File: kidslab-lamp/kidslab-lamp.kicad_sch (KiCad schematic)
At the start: 1 part

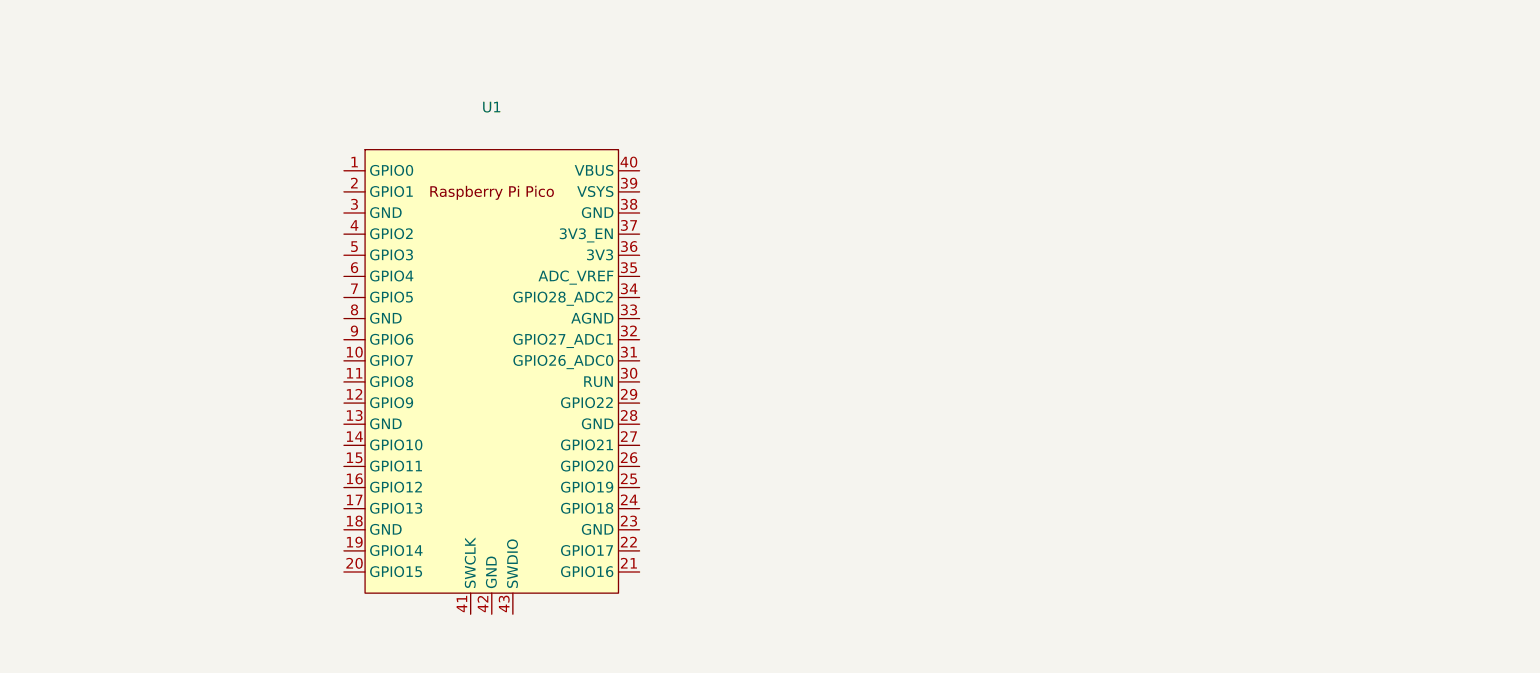
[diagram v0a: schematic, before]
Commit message: new pcb outline, added frisbee footprints, smaller PCB, added arrow footprints etc.
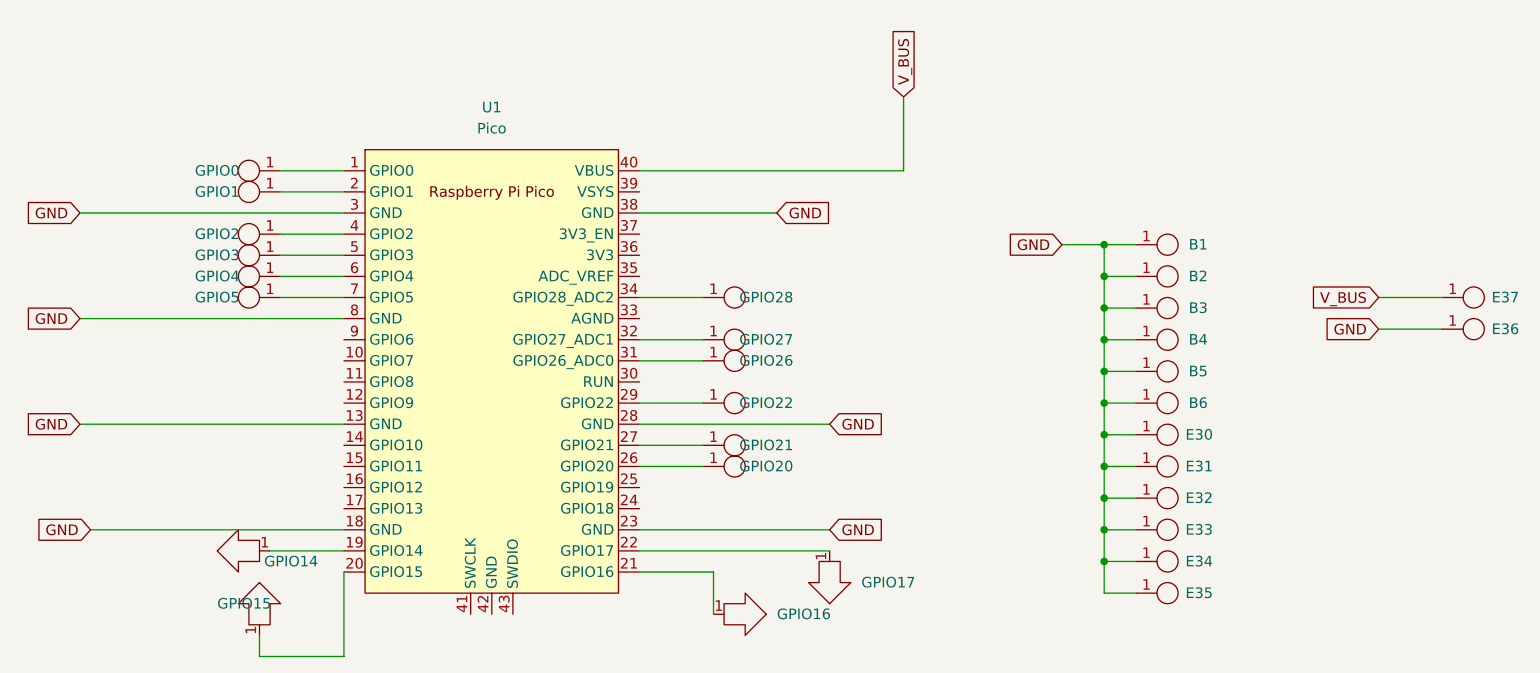
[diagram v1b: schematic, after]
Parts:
- added B1, B2, B3, B4, B5, B6: kroko_board, kidslab:KrokoConnector, symbol kidslab:kroko_board
- added E30, E31, E32, E33, E34, E35, E36, E37, GPIO0, GPIO1, GPIO2, GPIO20, GPIO21, GPIO22, GPIO26, GPIO27, GPIO28, GPIO3, GPIO4, GPIO5: kroko_edge, kidslab:Edgeconnector, symbol kidslab:kroko_edge
- added GPIO14, GPIO15, GPIO16, GPIO17: arrow, kidslab:Kroko_Arrow, symbol kidslab:arrow
- U1: value (none) -> Pico; footprint (none) -> pi-pico:RPi_Pico_SMD_TH
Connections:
- net at U1.1 (GPIO0): now also GPIO0.1
- net GND: now reaches U1.13 (GND)
- net GND: now also U1.18 (GND), U1.23 (GND), U1.28 (GND), U1.3 (GND), U1.38 (GND), U1.8 (GND), B1.1, B2.1, B3.1, B4.1, B5.1, B6.1, E30.1, E31.1, E32.1, E33.1, E34.1, E35.1, E36.1
- net at U1.19 (GPIO14): now also GPIO14.1
- net at U1.2 (GPIO1): now also GPIO1.1
- net at U1.20 (GPIO15): now also GPIO15.1
- net at U1.21 (GPIO16): now also GPIO16.1
- net at U1.22 (GPIO17): now also GPIO17.1
- net at U1.26 (GPIO20): now also GPIO20.1
- net at U1.27 (GPIO21): now also GPIO21.1
- net at U1.29 (GPIO22): now also GPIO22.1
- net at U1.31 (GPIO26_ADC0): now also GPIO26.1
- net at U1.32 (GPIO27_ADC1): now also GPIO27.1
- net at U1.34 (GPIO28_ADC2): now also GPIO28.1
- net at U1.4 (GPIO2): now also GPIO2.1
- net V_BUS: now reaches U1.40 (VBUS)
- net V_BUS: now also E37.1
- net at U1.5 (GPIO3): now also GPIO3.1
- net at U1.6 (GPIO4): now also GPIO4.1
- net at U1.7 (GPIO5): now also GPIO5.1

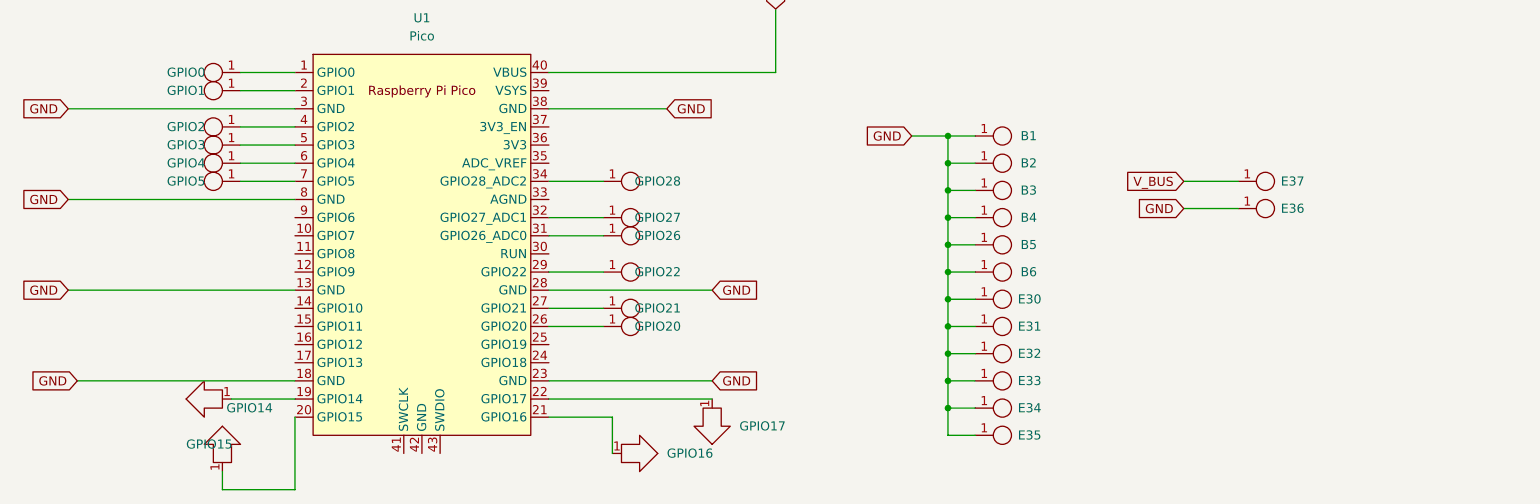
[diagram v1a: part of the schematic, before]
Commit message: added 3.3V rail, replaced GND on bottom with 5V rail added Servo pin header
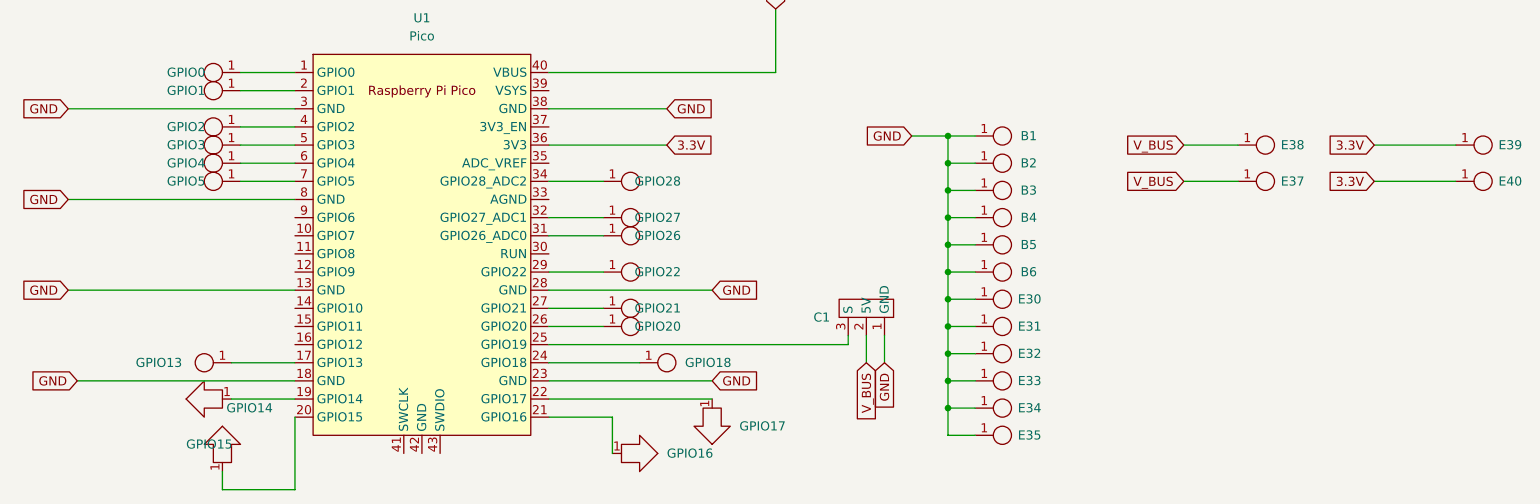
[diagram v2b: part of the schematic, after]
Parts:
- removed E36: kroko_edge, kidslab:Edgeconnector, symbol kidslab:kroko_edge
- added C1: (no value), symbol kidslab:pin_header_1x3
- added E38, E39, E40: kroko_edge, kidslab:Edgeconnector, symbol kidslab:kroko_edge
- added GPIO13, GPIO18: kroko_board, kidslab:KrokoConnector, symbol kidslab:kroko_board
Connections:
- net GND: now also C1.1 (GND)
- net V_BUS: now also C1.2 (5V), E38.1
- net at U1.17 (GPIO13): now also GPIO13.1
- net at U1.24 (GPIO18): now also GPIO18.1
- net at U1.25 (GPIO19): now also C1.3 (S)
- net 3.3V: now reaches U1.36 (3V3)
- net 3.3V: now also E39.1, E40.1

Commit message: added backside art, LED, and frontside kidslab logo
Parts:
- added D12: SK6812, LED_SMD:LED_SK6812_PLCC4_5.0x5.0mm_P3.2mm, symbol LED:SK6812
- C1: value (none) -> pin_header_1x3; footprint (none) -> Connector_PinHeader_2.54mm:PinHeader_1x03_P2.54mm_Vertical
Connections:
- net GND: now also D12.1 (VSS)
- net V_BUS: now also D12.3 (VDD)
- net at U1.16 (GPIO12): now also D12.2 (DIN)
- no-connect marks 0 -> 1
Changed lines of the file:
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@@
   (junction (at 185.42 93.98) (diameter 0) (color 0 0 0 0)
   )
+  (no_connect (at 25.4 92.71))
   (wire (pts (xy 185.42 67.31) (xy 185.42 71.12))
     (stroke (width 0) (type default) (color 0 0 0 0))
@@
     (stroke (width 0) (type default) (color 0 0 0 0))
   )
+  (wire (pts (xy 33.02 85.09) (xy 33.02 81.28))
+    (stroke (width 0) (type default) (color 0 0 0 0))
+  )
   (wire (pts (xy 185.42 82.55) (xy 185.42 86.36))
     (stroke (width 0) (type default) (color 0 0 0 0))
@@
     (stroke (width 0) (type default) (color 0 0 0 0))
   )
+  (wire (pts (xy 33.02 106.68) (xy 33.02 100.33))
+    (stroke (width 0) (type default) (color 0 0 0 0))
+  )
   (wire (pts (xy 185.42 74.93) (xy 185.42 78.74))
     (stroke (width 0) (type default) (color 0 0 0 0))
@@
     (stroke (width 0) (type default) (color 0 0 0 0))
   )
+  (wire (pts (xy 40.64 92.71) (xy 93.98 92.71))
+    (stroke (width 0) (type default) (color 0 0 0 0))
+  )
   (wire (pts (xy 129.54 87.63) (xy 137.16 87.63))
     (stroke (width 0) (type default) (color 0 0 0 0))
@@
     (stroke (width 0) (type default) (color 0 0 0 0))
   )
+  (wire (pts (xy 44.45 106.68) (xy 33.02 106.68))
+    (stroke (width 0) (type default) (color 0 0 0 0))
+  )
   (wire (pts (xy 189.23 90.17) (xy 185.42 90.17))
     (stroke (width 0) (type default) (color 0 0 0 0))
@@
   )
   (wire (pts (xy 161.29 45.72) (xy 161.29 54.61))
+    (stroke (width 0) (type default) (color 0 0 0 0))
+  )
+  (wire (pts (xy 46.99 81.28) (xy 33.02 81.28))
     (stroke (width 0) (type default) (color 0 0 0 0))
   )
@@
     )
   )
+  (global_label "V_BUS" (shape input) (at 44.45 106.68 0) (fields_autoplaced)
+    (effects (font (size 1.27 1.27)) (justify left))
+    (property "Intersheet References" "${INTERSHEET_REFS}" (id 0) (at 52.7293 106.6006 0)
+      (effects (font (size 1.27 1.27)) (justify left) hide)
+    )
+  )
   (global_label "3.3V" (shape input) (at 146.05 64.77 0) (fields_autoplaced)
     (effects (font (size 1.27 1.27)) (justify left))
@@
     (effects (font (size 1.27 1.27)) (justify left))
     (property "Intersheet References" "${INTERSHEET_REFS}" (id 0) (at 161.2106 37.4407 90)
+      (effects (font (size 1.27 1.27)) (justify left) hide)
+    )
+  )
+  (global_label "GND" (shape input) (at 46.99 81.28 0) (fields_autoplaced)
+    (effects (font (size 1.27 1.27)) (justify left))
+    (property "Intersheet References" "${INTERSHEET_REFS}" (id 0) (at 53.2736 81.2006 0)
       (effects (font (size 1.27 1.27)) (justify left) hide)
     )
@@
     (pin "1")
   )
+  (symbol (lib_id "LED:SK6812") (at 33.02 92.71 180) (unit 1)
+    (in_bom yes) (on_board yes) (fields_autoplaced)
+    (property "Reference" "D12" (id 0) (at 43.18 86.8805 0))
+    (property "Value" "SK6812" (id 1) (at 43.18 89.4205 0))
+    (property "Footprint" "LED_SMD:LED_SK6812_PLCC4_5.0x5.0mm_P3.2mm" (id 2) (at 31.75 85.09 0)
+      (effects (font (size 1.27 1.27)) (justify left top) hide)
+    )
+    (property "Datasheet" "https://cdn-shop.adafruit.com/product-files/1138/SK6812+LED+datasheet+.pdf" (id 3) (at 30.48 83.185 0)
+      (effects (font (size 1.27 1.27)) (justify left top) hide)
+    )
+    (pin "1")
+    (pin "2")
+    (pin "3")
+    (pin "4")
+  )
   (symbol (lib_id "kidslab:kroko_edge") (at 191.77 93.98 0) (unit 1)
     (in_bom no) (on_board yes)
@@
       (effects (font (size 1.27 1.27)) (justify left))
     )
-    (property "Value" "" (id 1) (at 180.34 82.55 0)
+    (property "Value" "pin_header_1x3" (id 1) (at 180.34 82.55 0)
       (effects (font (size 1.27 1.27)) (justify left))
     )
-    (property "Footprint" "" (id 2) (at 172.72 80.01 0)
+    (property "Footprint" "Connector_PinHeader_2.54mm:PinHeader_1x03_P2.54mm_Vertical" (id 2) (at 172.72 80.01 0)
       (effects (font (size 1.27 1.27)) hide)
     )
@@
       (reference "C1") (unit 1) (value "pin_header_1x3") (footprint "Connector_PinHeader_2.54mm:PinHeader_1x03_P2.54mm_Vertical")
     )
+    (path "/811f5389-c208-4640-ab1a-b454491bb330"
+      (reference "D12") (unit 1) (value "SK6812") (footprint "LED_SMD:LED_SK6812_PLCC4_5.0x5.0mm_P3.2mm")
+    )
     (path "/68dec79b-1b47-40e3-b6bd-cbd6d65297a7"

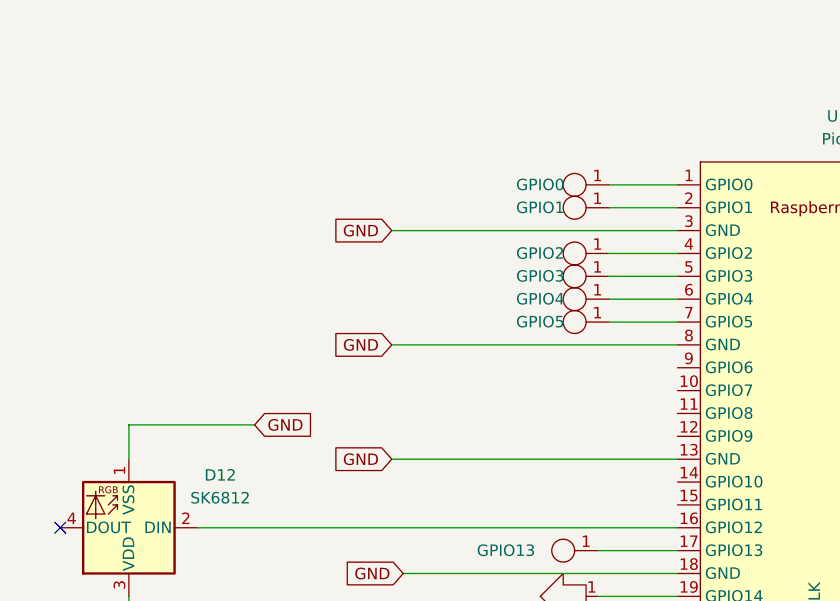
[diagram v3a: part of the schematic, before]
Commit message: finished design, further checks have to be done before ordering
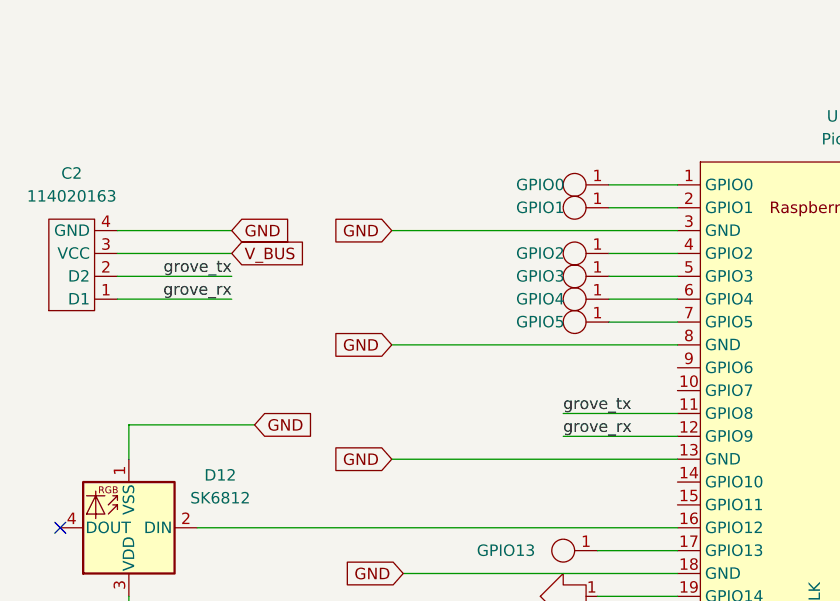
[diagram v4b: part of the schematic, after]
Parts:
- added C2: 114020163, kidslab:114020163, symbol kidslab:114020163
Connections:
- net GND: now also C2.4 (GND)
- net V_BUS: now also C2.3 (VCC)
- net grove_tx: now reaches U1.11 (GPIO8)
- net grove_tx: now also C2.2 (D2)
- net grove_rx: now reaches U1.12 (GPIO9)
- net grove_rx: now also C2.1 (D1)
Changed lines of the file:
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@@
+    (stroke (width 0) (type default) (color 0 0 0 0))
+  )
+  (wire (pts (xy 44.45 64.77) (xy 31.75 64.77))
+    (stroke (width 0) (type default) (color 0 0 0 0))
+  )
+  (wire (pts (xy 44.45 67.31) (xy 31.75 67.31))
     (stroke (width 0) (type default) (color 0 0 0 0))
   )
@@
     (stroke (width 0) (type default) (color 0 0 0 0))
   )
+  (wire (pts (xy 81.28 82.55) (xy 93.98 82.55))
+    (stroke (width 0) (type default) (color 0 0 0 0))
+  )
   (wire (pts (xy 189.23 82.55) (xy 185.42 82.55))
     (stroke (width 0) (type default) (color 0 0 0 0))
@@
     (stroke (width 0) (type default) (color 0 0 0 0))
   )
+  (wire (pts (xy 81.28 80.01) (xy 93.98 80.01))
+    (stroke (width 0) (type default) (color 0 0 0 0))
+  )
   (wire (pts (xy 245.11 64.77) (xy 256.54 64.77))
     (stroke (width 0) (type default) (color 0 0 0 0))
@@
     (stroke (width 0) (type default) (color 0 0 0 0))
   )
+  (wire (pts (xy 44.45 62.23) (xy 31.75 62.23))
+    (stroke (width 0) (type default) (color 0 0 0 0))
+  )
   (wire (pts (xy 180.34 63.5) (xy 185.42 63.5))
     (stroke (width 0) (type default) (color 0 0 0 0))
@@
     (stroke (width 0) (type default) (color 0 0 0 0))
   )
+  (wire (pts (xy 44.45 59.69) (xy 31.75 59.69))
+    (stroke (width 0) (type default) (color 0 0 0 0))
+  )
   (wire (pts (xy 189.23 97.79) (xy 185.42 97.79))
     (stroke (width 0) (type default) (color 0 0 0 0))
@@
   (wire (pts (xy 185.42 101.6) (xy 185.42 105.41))
     (stroke (width 0) (type default) (color 0 0 0 0))
+  )
+  (label "grove_tx" (at 81.28 80.01 0)
+    (effects (font (size 1.27 1.27)) (justify left bottom))
+  )
+  (label "grove_tx" (at 44.45 64.77 180)
+    (effects (font (size 1.27 1.27)) (justify right bottom))
+  )
+  (label "grove_rx" (at 44.45 67.31 180)
+    (effects (font (size 1.27 1.27)) (justify right bottom))
+  )
+  (label "grove_rx" (at 81.28 82.55 0)
+    (effects (font (size 1.27 1.27)) (justify left bottom))
   )
   (global_label "V_BUS" (shape input) (at 173.99 95.25 270) (fields_autoplaced)
@@
     )
   )
+  (global_label "V_BUS" (shape input) (at 44.45 62.23 0) (fields_autoplaced)
+    (effects (font (size 1.27 1.27)) (justify left))
+    (property "Intersheet References" "${INTERSHEET_REFS}" (id 0) (at 52.7293 62.1506 0)
+      (effects (font (size 1.27 1.27)) (justify left) hide)
+    )
+  )
   (global_label "GND" (shape input) (at 180.34 63.5 180) (fields_autoplaced)
     (effects (font (size 1.27 1.27)) (justify right))
     (property "Intersheet References" "${INTERSHEET_REFS}" (id 0) (at 174.0564 63.5794 0)
       (effects (font (size 1.27 1.27)) (justify right) hide)
+    )
+  )
+  (global_label "GND" (shape input) (at 44.45 59.69 0) (fields_autoplaced)
+    (effects (font (size 1.27 1.27)) (justify left))
+    (property "Intersheet References" "${INTERSHEET_REFS}" (id 0) (at 50.7336 59.6106 0)
+      (effects (font (size 1.27 1.27)) (justify left) hide)
     )
   )
@@
     (pin "1")
   )
+  (symbol (lib_id "kidslab:114020163") (at 29.21 63.5 90) (unit 1)
+    (in_bom yes) (on_board yes) (fields_autoplaced)
+    (property "Reference" "C2" (id 0) (at 26.67 53.34 90))
+    (property "Value" "114020163" (id 1) (at 26.67 55.88 90))
+    (property "Footprint" "kidslab:114020163" (id 2) (at 29.21 63.5 0)
+      (effects (font (size 1.27 1.27)) hide)
+    )
+    (property "Datasheet" "https://www.mouser.de/datasheet/2/744/Grove_Female_Header_-_SMD-4P-2.0mm_Datasheet-1853538.pdf" (id 3) (at 20.32 63.5 0)
+      (effects (font (size 1.27 1.27)) hide)
+    )
+    (pin "1")
+    (pin "2")
+    (pin "3")
+    (pin "4")
+  )
   (symbol (lib_id "LED:SK6812") (at 33.02 92.71 180) (unit 1)
     (in_bom yes) (on_board yes) (fields_autoplaced)
@@
       (reference "C1") (unit 1) (value "pin_header_1x3") (footprint "Connector_PinHeader_2.54mm:PinHeader_1x03_P2.54mm_Vertical")
     )
+    (path "/6ce63d0b-9f98-4735-b97b-dbcb0f8c7222"
+      (reference "C2") (unit 1) (value "114020163") (footprint "kidslab:114020163")
+    )
     (path "/811f5389-c208-4640-ab1a-b454491bb330"

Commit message: updated PCB with requested changes
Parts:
- removed GPIO20, GPIO5: kroko_edge, kidslab:Edgeconnector, symbol kidslab:kroko_edge
- added C3: pin_header_1x3, Connector_PinHeader_2.54mm:PinHeader_1x03_P2.54mm_Vertical, symbol kidslab:pin_header_1x3
- added R1, R2, R3, R4: 10M, Resistor_THT:R_Axial_DIN0204_L3.6mm_D1.6mm_P5.08mm_Horizontal, symbol Device:R
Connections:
- net 3.3V: now also D12.3 (VDD), R1.2, R2.2, R3.2, R4.2
- net GND: now also C3.1 (GND)
- net V_BUS: now also C3.2 (5V); no longer D12.3 (VDD)
- net at U1.14 (GPIO10): now also C1.3 (S)
- net at U1.15 (GPIO11): now also C3.3 (S)
- net at GPIO14.1, U1.19 (GPIO14): now also R1.1
- net at GPIO15.1, U1.20 (GPIO15): now also R2.1
- net at GPIO16.1, U1.21 (GPIO16): now also R3.1
- net at GPIO17.1, U1.22 (GPIO17): now also R4.1
- net at U1.25 (GPIO19): no longer C1.3 (S)
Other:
- moved on the sheet: C1, D12, GPIO14, GPIO15, GPIO16, GPIO17

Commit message: cleared schematics and exported pdf, fixed some routing issues, generated gerber files
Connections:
- net GPIO11: now reaches C3.3 (S), U1.15 (GPIO11)
- net GPIO16: now reaches GPIO16.1, R3.1, U1.21 (GPIO16)
- net GPIO10: now reaches C1.3 (S), U1.14 (GPIO10)
- net GPIO12: now reaches D12.2 (DIN), U1.16 (GPIO12)
- net GPIO14: now reaches GPIO14.1, R1.1, U1.19 (GPIO14)
- net GPIO15: now reaches GPIO15.1, R2.1, U1.20 (GPIO15)
- net GPIO17: now reaches GPIO17.1, R4.1, U1.22 (GPIO17)
- no-connect marks 1 -> 6
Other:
- note added: "(5 V)"
- note added: "Grove"
- note added: "LED"
- note added: "Pfeiltasten"
- note added: "Power-Groko"
- note added: "Servo-Anschlüsse"
- moved on the sheet: B1, B2, B3, B4, B5, B6, C1, C2, C3, D12, E30, E31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
